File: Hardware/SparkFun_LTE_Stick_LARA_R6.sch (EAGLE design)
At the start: 75 parts, among them IC1 SN74AVC4T774PW, IC3 SN74AVC4T774PW, J1 NANO_SIM, U1 LARA-R6401, U2 AP7361C-33

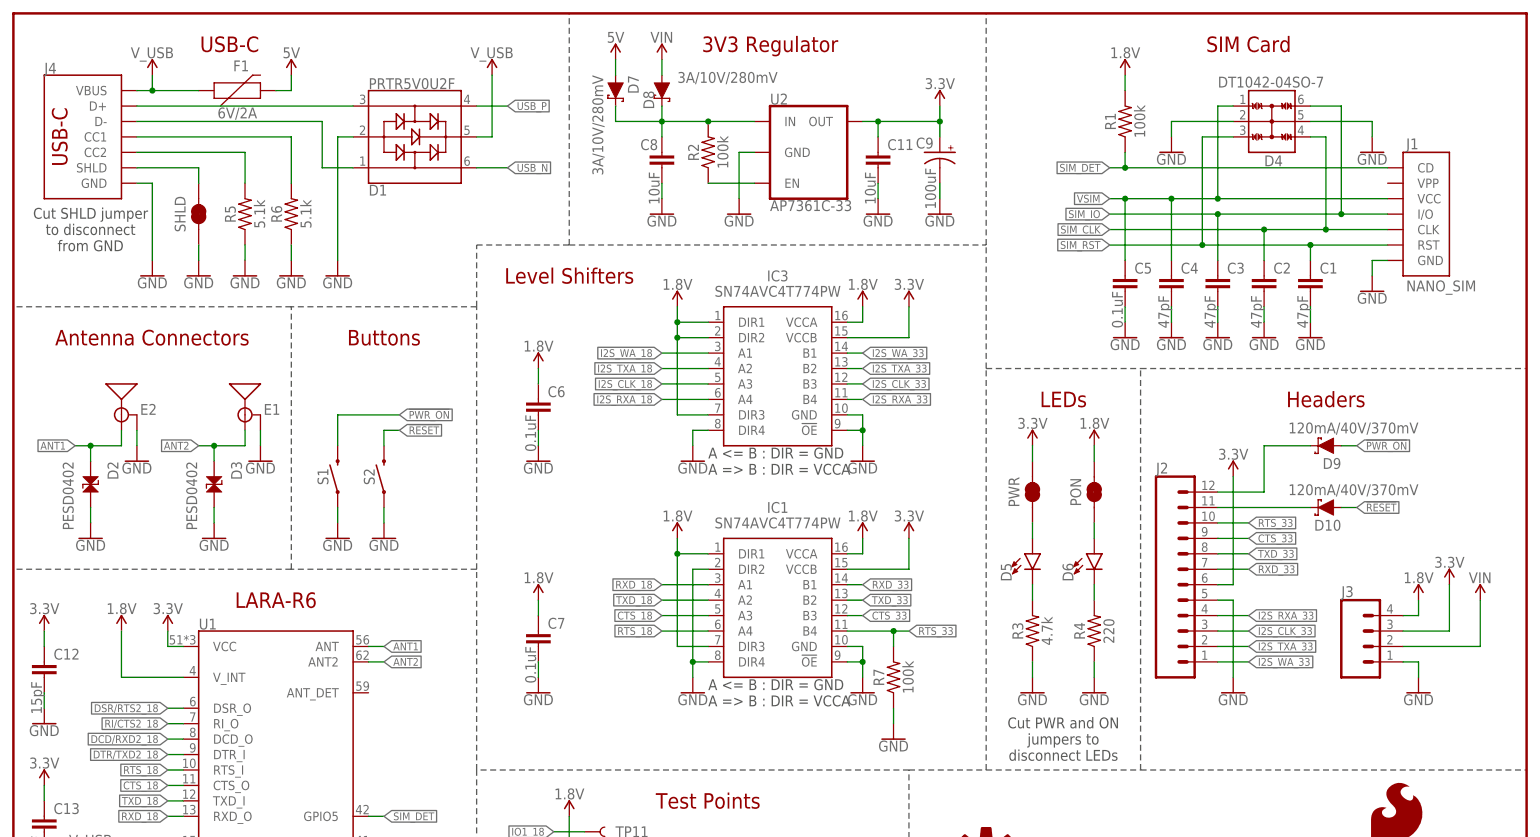
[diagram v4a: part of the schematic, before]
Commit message: Design review updates
Update Eagle libraries to fix vector fonts for some symbols
Add GND vias near SIM holder pads
Add max input voltage for VREG
Straighten USB trace near connector (N$10)
Fix trace on ANT1 ESD pad
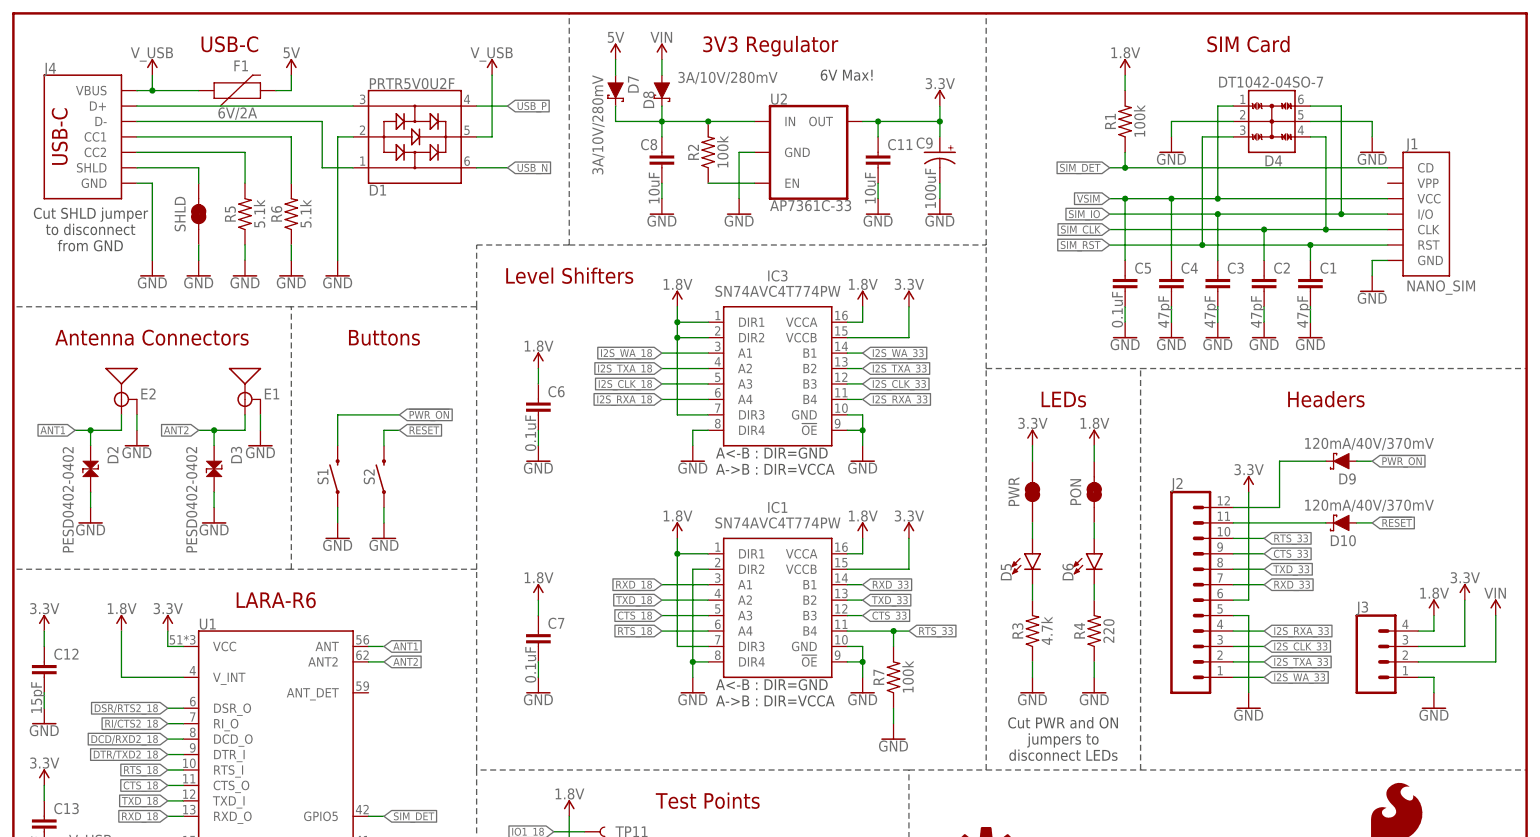
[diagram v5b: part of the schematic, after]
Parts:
- D2, D3: value PESD0402 -> PESD0402-0402; device SparkFun-DiscreteSemi:PESD0402 -> SparkFun-DiscreteSemi:PESD0402-0402
- D4: device SparkFun-DiscreteSemi:TVS_DIODE_ARRAY_4DT1042-04SO-7 -> SparkFun-DiscreteSemi:TVS_DIODE_ARRAY_4_ESDA6V1BC6
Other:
- note added: "6V Max!"
- moved on the sheet: D10, D9, E1, E2, IC1, IC3, J2, J3

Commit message: Clean up design
Increase frame to ledger size
Arrange test points in schematic to match physical layout
Add impedance calculations to schematic
Update LED VALUE attributes with color in schematic
Add silkscreen labels to test points
Decrease font size of top buzzard labels to make tails more visible
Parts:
- D5, D6: value (none) -> Red
- FRAME1: value FRAME-LETTER -> FRAME-LEDGER; device SparkFun-Aesthetics:FRAME-LETTER -> SparkFun-Aesthetics:FRAME-LEDGER
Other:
- note added: "Differential Pair Calculation:"
- note added: "GND test point labeled as pin 1"
- note added: "GPIO cluster"
- note added: "I2C cluster"
- note added: "Total Copper Thickness: 1.4mil / 36um Material: FR-4 STD Er:4.6 Conductor Width: 12.3mil / 0.31mm Conductor Gap: 7mil / 0.18mm JLC-7628 Prepreg dielectric thickness: 0.180mm (7.1mil) 4-LAYER Z: 50.0 Ohms http://saturnpcb.com/pcb_toolkit/"
- note added: "Total Copper Thickness: 1.4mil / 36um Material: FR-4 STD Er:4.6 Conductor Width: 9.42mil / 0.24mm Conductor Spacing: 7mil / 0.18mm JLC-7628 Prepreg dielectric thickness: 0.180mm (7.1mil) 4-LAYER Zdifferential: 90.0 Ohms http://saturnpcb.com/pcb_toolkit/"
- note added: "UART2 cluster"
- moved on the sheet: C1, C10, C11, C12, C13, C2, C3, C4, C5, C6, C7, C8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

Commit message: v10 updates
Bump version number to v10
Add AT Commands Manual
Add Application Development App Note
Add Audio App Note
Fix text in Antenna Connectors section to be "Coplanar Waveguide Calculation"
Reposition D7 and D8 so text is horizontal
Change material to TG155 in ordering instructions
Nudge some vias to avoid silk
Shrink pin label size to 0.0375 so flags are visible
Replace PON with ON
Appaned "_LED" to LED jumpers
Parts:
- FRAME1: REV v01 -> v10
- renumbered PON to ON_LED, PWR to PWR_LED, S1 to ON_BTN, S2 to RST_BTN
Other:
- note added: "Coplanar Waveguide Calculation:"
- moved on the sheet: D7, D8

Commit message: Change SMA connector PROD_ID
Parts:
- E1, E2: PROD_ID (none) -> CONN-19593
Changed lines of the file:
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@@
 </classes>
 <parts>
-<part name="E1" library="SparkFun-RF" deviceset="ANTENNA-SMA-GROUNDED" device="EDGE_SMA"/>
-<part name="E2" library="SparkFun-RF" deviceset="ANTENNA-SMA-GROUNDED" device="EDGE_SMA"/>
+<part name="E1" library="SparkFun-RF" deviceset="ANTENNA-SMA-GROUNDED" device="EDGE_SMA">
+<attribute name="PROD_ID" value="CONN-19593"/>
+</part>
+<part name="E2" library="SparkFun-RF" deviceset="ANTENNA-SMA-GROUNDED" device="EDGE_SMA">
+<attribute name="PROD_ID" value="CONN-19593"/>
+</part>
 <part name="J4" library="SparkFun-Connectors" deviceset="USB_C" device="_4-LAYER_PADS"/>
 <part name="H1" library="SparkFun-Hardware" deviceset="STAND-OFF" device=""/>
